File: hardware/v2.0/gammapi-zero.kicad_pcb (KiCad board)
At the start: 4 copper layers, 65 x 30 mm, 206 parts, among them IC1 IS42S16160J-6BLI-TR, IC2 ADA4932-1YCPZ-R7, IC3 LM4040AIM3-2.0_NOPB, IC4 LTC2622IMS8#PBF, IC6 ADS6122IRHBT, J1 Conn_02x20_Counter_Clockwise, J2 GPDI_C_1.3, J3 USB_C_Receptacle_USB2.0_14P, J4 USB_C_Receptacle_USB2.0_14P, J5 USB_C_Receptacle_USB2.0_14P, J6 Micro_SD_Card_Det2, J7 RSP-122811-01, J8 GT-A1201WRS-104B1101, SW1 SW_Push, SW2 SW_Push, U1 ECP5U-25F-CABGA256, U10 TPD2EUSB30A, U12 W25Q128JVS, U2 TLV62569DBV, U3 TLV62569DBV, U4 TLV62569DBV, U6 PCA9306DC1, U7 TPD2EUSB30A, U8 TPD2EUSB30A, U9 FT231XQ, Y1 SG-8018CG 50.000000MHz, Y2 SG-8018CG 50.000000MHz

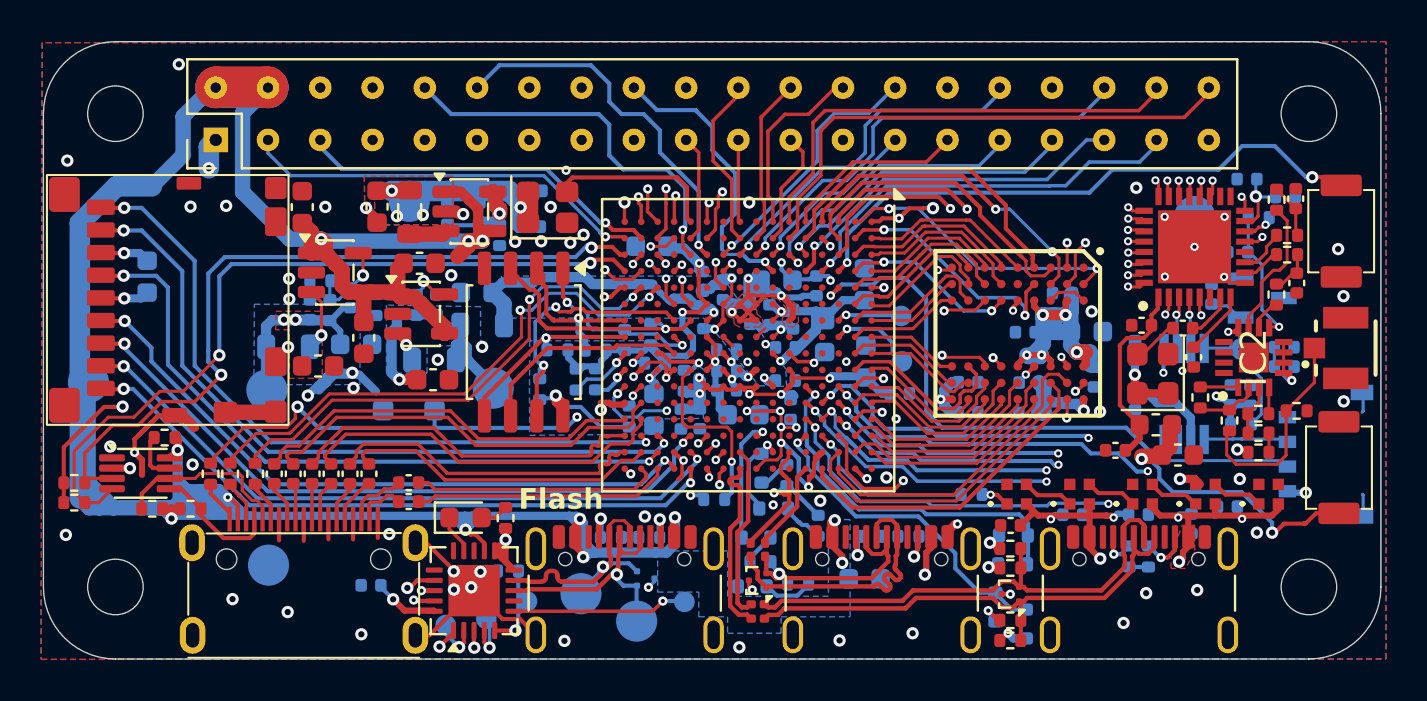
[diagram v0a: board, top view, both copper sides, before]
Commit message: WS2812B-2020 LED Update
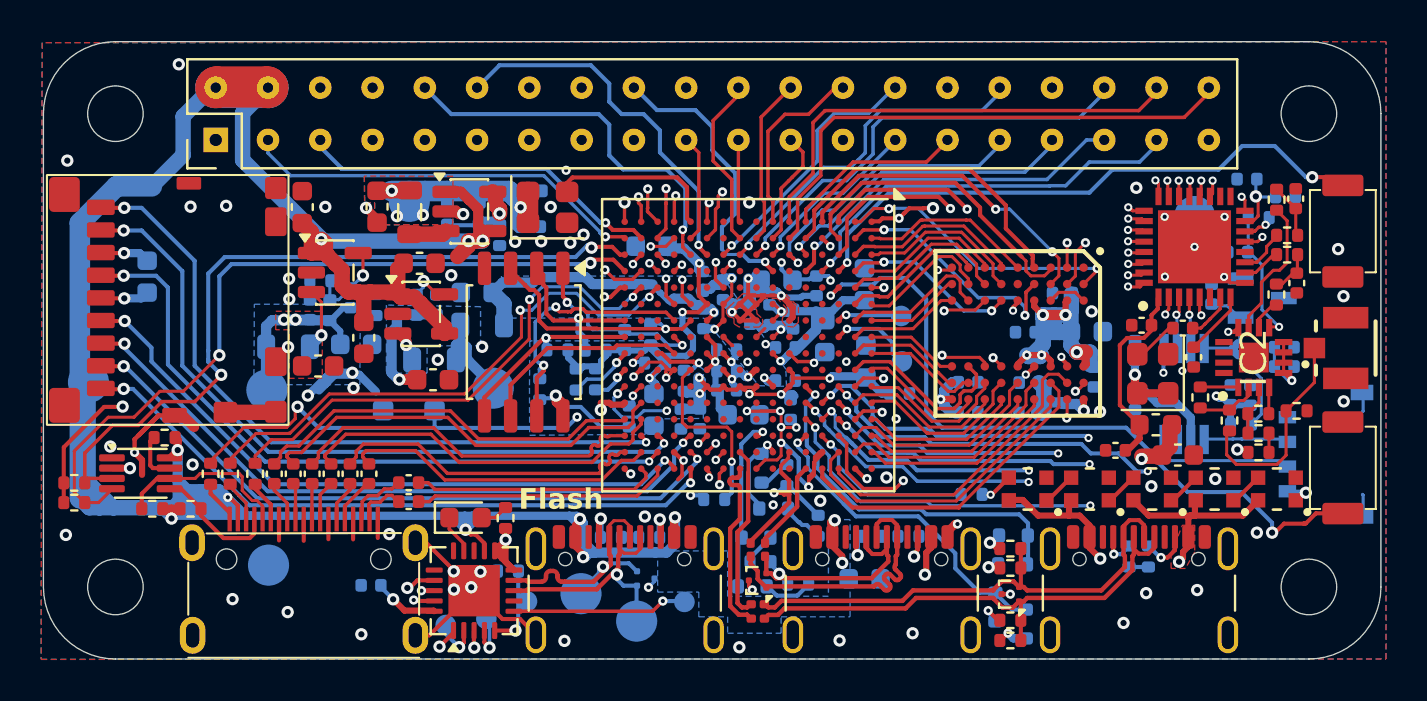
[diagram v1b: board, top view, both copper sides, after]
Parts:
- removed C68, C70, C71, C72, C73: 100n, Capacitor_SMD:C_0402_1005Metric
- LED1, LED2, LED3, LED4, LED5: value IN-PI15TAT5R5G5B -> WS2812B2020; footprint IN-PI15TAT5R5G5B:INPI15TAT5R5G5B -> WS2812B2020:LED_WS2812B2020
- moved LED1 0.59 mm to (163.6, 111.7), turned to 180 degrees
- moved LED2 0.56 mm to (166.6, 111.7), turned to 180 degrees
- moved LED3 0.53 mm to (169.6, 111.7), turned to 180 degrees
- moved LED4 0.51 mm to (172.7, 111.7), turned to 180 degrees
- moved LED5 0.48 mm to (175.7, 111.7), turned to 180 degrees
- moved SW2 0.19 mm to (178.9, 110.7)
- moved SW1 0.08 mm to (178.9, 99.2)
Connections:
- LED1 pad 1: Net-(LED1-DIN) -> Net-(LED1-DO)
- LED1 pad 2: +5V -> GND
- LED1 pad 3: Net-(LED1-DOUT) -> Net-(LED1-DI)
- LED1 pad 4: GND -> +5V
- LED2 pad 1: Net-(LED1-DOUT) -> Net-(LED2-DO)
- LED2 pad 2: +5V -> GND
- LED2 pad 3: Net-(LED2-DOUT) -> Net-(LED1-DO)
- LED2 pad 4: GND -> +5V
- LED3 pad 1: Net-(LED2-DOUT) -> Net-(LED3-DO)
- LED3 pad 2: +5V -> GND
- LED3 pad 3: Net-(LED3-DOUT) -> Net-(LED2-DO)
- LED3 pad 4: GND -> +5V
- LED4 pad 1: Net-(LED3-DOUT) -> Net-(LED4-DO)
- LED4 pad 2: +5V -> GND
- LED4 pad 3: Net-(LED4-DOUT) -> Net-(LED3-DO)
- LED4 pad 4: GND -> +5V
- LED5 pad 1: Net-(LED4-DOUT) -> unconnected-(LED5-DO-Pad1)
- LED5 pad 2: +5V -> GND
- LED5 pad 3: unconnected-(LED5-DOUT-Pad3) -> Net-(LED4-DO)
- LED5 pad 4: GND -> +5V
- R1 pad 1: Net-(LED1-DIN) -> Net-(LED1-DI)
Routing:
- net +5V: track 220.6 -> 215.9 mm, vias 19 -> 15
- net Net-(LED4-DOUT): track 2.48 -> 0.00 mm
- net Net-(LED3-DOUT): track 2.45 -> 0.00 mm
- net Net-(LED2-DOUT): track 2.45 -> 0.00 mm
- net Net-(LED1-DOUT): track 2.45 -> 0.00 mm
- net Net-(LED2-DO): track 0.00 -> 1.66 mm
- net Net-(LED3-DO): track 0.00 -> 1.66 mm
- net Net-(LED1-DO): track 0.00 -> 1.66 mm
- net Net-(LED4-DO): track 0.00 -> 1.66 mm
- net +3V3: track 141.2 -> 139.7 mm, vias 35 -> 34
- net Net-(LED1-DI): track 0.00 -> 1.37 mm, vias 0 -> 1
- net Net-(LED1-DIN): track 1.32 -> 0.00 mm, vias 1 -> 0
- net GND: track 98.9 -> 97.8 mm
- net /ADC/PDN: track 36.1 -> 35.6 mm

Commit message: Capacitor update
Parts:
- C62: footprint Capacitor_SMD:C_0603_1608Metric -> Capacitor_SMD:C_0402_1005Metric
- moved C62 0.16 mm to (170.9, 109.9)
- moved R57 0.15 mm to (172.0, 107.1)
